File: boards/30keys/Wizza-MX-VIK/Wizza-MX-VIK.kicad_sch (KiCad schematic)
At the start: 88 parts, among them J1 AudioJack4dpb, J2 AudioJack4dpb, J3 Conn_01x03_Socket, J4 Conn_01x03_Socket, J7 Conn_01x05, J8 Conn_01x05, SW1 SW_Push, SW10 SW_Push, SW11 SW_Push, SW12 SW_Push, SW13 SW_Push, SW14 SW_Push, SW15 SW_Push, SW16 SW_Push, SW17 SW_Push, SW18 SW_Push, SW19 SW_Push, SW2 SW_Push, SW20 SW_Push, SW21 SW_Push, SW22 SW_Push, SW23 SW_Push, SW24 SW_Push, SW25 SW_SPDT, SW26 SW_Push, SW27 SW_Push, SW28 SW_Push, SW29 SW_Push, SW3 SW_Push, SW30 SW_SPDT, SW31 SW_Push, SW32 SW_Push, SW33 SW_Push, SW34 Rotary_Encoder_Switch, SW35 Rotary_Encoder_Switch, SW4 SW_Push, SW40 SW_Push, SW5 SW_Push, SW6 SW_Push, SW7 SW_Push, SW8 SW_Push, SW9 SW_Push, U1 Helios, U2 Helios

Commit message: wizza mx vik
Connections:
- net ENC_L_L is gone; now on net EncL_L: SW34.A
- net ENC_L_R is gone; now on net EncL_R: SW35.B
- net ENC_R_L is gone; now on net EncR_L: SW34.B
- net ENC_R_R is gone; now on net EncR_R: SW35.A
- net MISO_L: now also J2.11 (MISO), J6.11 (MISO)
- net MISO_R: now also J1.11 (MISO), J5.11 (MISO)
- net MOSI_L: no longer J2.11 (MISO), J6.11 (MISO)
- net MOSI_R: no longer J1.11 (MISO), J5.11 (MISO)
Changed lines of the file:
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@@
+    )
+  )
+  (global_label "MISO_R" (shape input) (at 386.08 82.55 180) (fields_autoplaced)
+    (effects (font (size 1.27 1.27)) (justify right))
+    (property "Intersheetrefs" "${INTERSHEET_REFS}" (at 376.3404 82.55 0)
+      (effects (font (size 1.27 1.27)) (justify right) hide)
     )
   )
@@
     )
   )
-  (global_label "MOSI_R" (shape input) (at 386.08 82.55 180) (fields_autoplaced)
-    (effects (font (size 1.27 1.27)) (justify right))
-    (property "Intersheetrefs" "${INTERSHEET_REFS}" (at 376.3404 82.55 0)
-      (effects (font (size 1.27 1.27)) (justify right) hide)
-    )
-  )
   (global_label "NCS_L" (shape input) (at 77.47 87.63 0) (fields_autoplaced)
     (effects (font (size 1.27 1.27)) (justify left))
@@
     )
   )
-  (global_label "MOSI_L" (shape input) (at 105.41 118.11 180) (fields_autoplaced)
-    (effects (font (size 1.27 1.27)) (justify right))
-    (property "Intersheetrefs" "${INTERSHEET_REFS}" (at 95.9123 118.11 0)
-      (effects (font (size 1.27 1.27)) (justify right) hide)
-    )
-  )
   (global_label "GND_L" (shape input) (at 179.07 153.67 0) (fields_autoplaced)
     (effects (font (size 1.27 1.27)) (justify left))
@@
     )
   )
-  (global_label "MOSI_R" (shape input) (at 386.08 116.84 180) (fields_autoplaced)
-    (effects (font (size 1.27 1.27)) (justify right))
-    (property "Intersheetrefs" "${INTERSHEET_REFS}" (at 376.3404 116.84 0)
-      (effects (font (size 1.27 1.27)) (justify right) hide)
-    )
-  )
   (global_label "GND_R" (shape input) (at 322.58 66.04 180) (fields_autoplaced)
     (effects (font (size 1.27 1.27)) (justify right))
@@
     )
   )
-  (global_label "ENC_L_R" (shape input) (at 287.02 231.14 270) (fields_autoplaced)
-    (effects (font (size 1.27 1.27)) (justify right))
-    (property "Intersheetrefs" "${INTERSHEET_REFS}" (at 287.02 242.0286 90)
+  (global_label "EncL_R" (shape input) (at 287.02 231.14 270) (fields_autoplaced)
+    (effects (font (size 1.27 1.27)) (justify right))
+    (property "Intersheetrefs" "${INTERSHEET_REFS}" (at 287.02 240.6981 90)
       (effects (font (size 1.27 1.27)) (justify right) hide)
     )
@@
     )
   )
+  (global_label "MISO_L" (shape input) (at 105.41 118.11 180) (fields_autoplaced)
+    (effects (font (size 1.27 1.27)) (justify right))
+    (property "Intersheetrefs" "${INTERSHEET_REFS}" (at 95.9123 118.11 0)
+      (effects (font (size 1.27 1.27)) (justify right) hide)
+    )
+  )
   (global_label "SCLK_R" (shape input) (at 358.14 78.74 0) (fields_autoplaced)
     (effects (font (size 1.27 1.27)) (justify left))
@@
     )
   )
-  (global_label "ENC_L_L" (shape input) (at 146.05 227.33 270) (fields_autoplaced)
-    (effects (font (size 1.27 1.27)) (justify right))
-    (property "Intersheetrefs" "${INTERSHEET_REFS}" (at 146.05 237.9767 90)
+  (global_label "EncL_L" (shape input) (at 146.05 227.33 270) (fields_autoplaced)
+    (effects (font (size 1.27 1.27)) (justify right))
+    (property "Intersheetrefs" "${INTERSHEET_REFS}" (at 146.05 236.6462 90)
       (effects (font (size 1.27 1.27)) (justify right) hide)
     )
@@
     )
   )
+  (global_label "MISO_R" (shape input) (at 386.08 116.84 180) (fields_autoplaced)
+    (effects (font (size 1.27 1.27)) (justify right))
+    (property "Intersheetrefs" "${INTERSHEET_REFS}" (at 376.3404 116.84 0)
+      (effects (font (size 1.27 1.27)) (justify right) hide)
+    )
+  )
   (global_label "EncL_R" (shape input) (at 322.58 60.96 180) (fields_autoplaced)
     (effects (font (size 1.27 1.27)) (justify right))
@@
     )
   )
-  (global_label "ENC_R_R" (shape input) (at 281.94 231.14 270) (fields_autoplaced)
-    (effects (font (size 1.27 1.27)) (justify right))
-    (property "Intersheetrefs" "${INTERSHEET_REFS}" (at 281.94 242.2705 90)
-      (effects (font (size 1.27 1.27)) (justify right) hide)
-    )
-  )
-  (global_label "ENC_R_L" (shape input) (at 151.13 227.33 270) (fields_autoplaced)
-    (effects (font (size 1.27 1.27)) (justify right))
-    (property "Intersheetrefs" "${INTERSHEET_REFS}" (at 151.13 238.2186 90)
-      (effects (font (size 1.27 1.27)) (justify right) hide)
-    )
-  )
-  (global_label "MOSI_L" (shape input) (at 105.41 83.82 180) (fields_autoplaced)
+  (global_label "EncR_R" (shape input) (at 281.94 231.14 270) (fields_autoplaced)
+    (effects (font (size 1.27 1.27)) (justify right))
+    (property "Intersheetrefs" "${INTERSHEET_REFS}" (at 281.94 240.94 90)
+      (effects (font (size 1.27 1.27)) (justify right) hide)
+    )
+  )
+  (global_label "EncR_L" (shape input) (at 151.13 227.33 270) (fields_autoplaced)
+    (effects (font (size 1.27 1.27)) (justify right))
+    (property "Intersheetrefs" "${INTERSHEET_REFS}" (at 151.13 236.8881 90)
+      (effects (font (size 1.27 1.27)) (justify right) hide)
+    )
+  )
+  (global_label "MISO_L" (shape input) (at 105.41 83.82 180) (fields_autoplaced)
     (effects (font (size 1.27 1.27)) (justify right))
     (property "Intersheetrefs" "${INTERSHEET_REFS}" (at 95.9123 83.82 0)

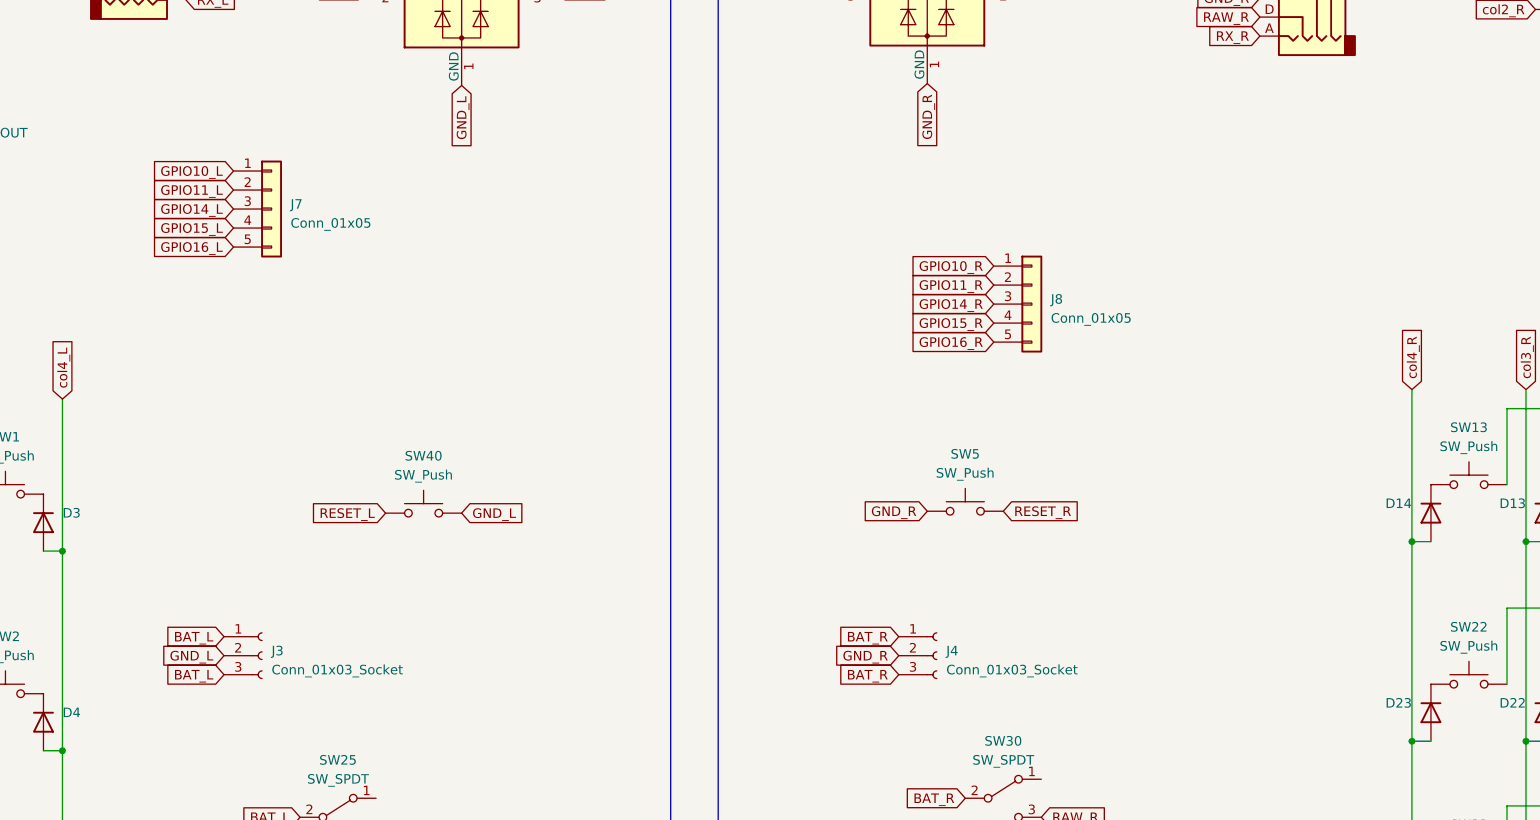
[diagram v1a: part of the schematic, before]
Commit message: add vik 18 pin ffc
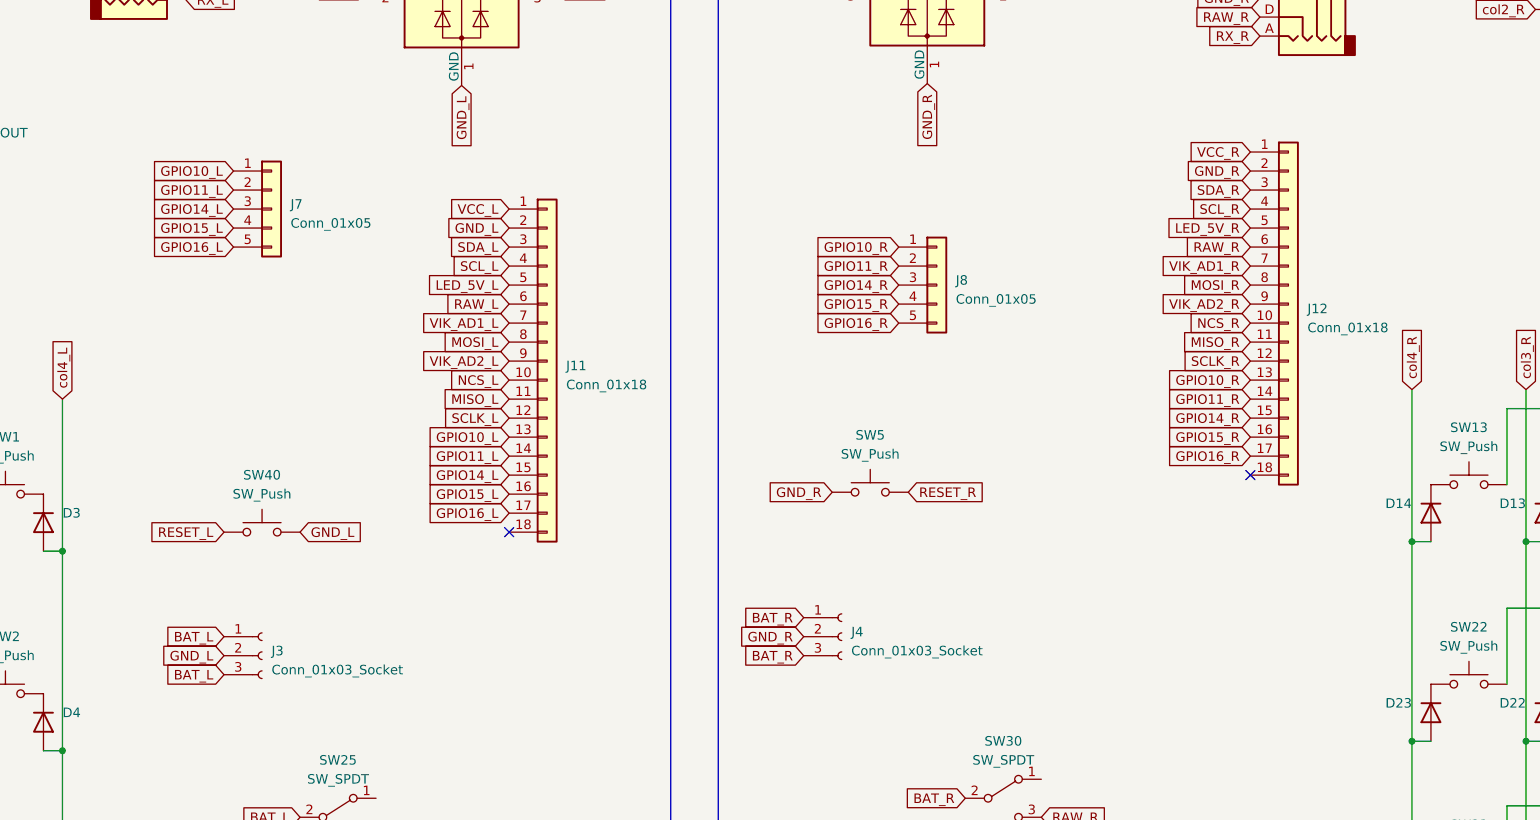
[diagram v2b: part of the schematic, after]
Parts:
- added J11, J12: Conn_01x18, Alaa:FPC-SMD_FPC05018-09200-.5mm-rev, symbol Connector_Generic:Conn_01x18
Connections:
- net GND_L: now also J11.2 (Pin_2)
- net GND_R: now also J12.2 (Pin_2)
- net GPIO10_L: now also J11.13 (Pin_13)
- net GPIO10_R: now also J12.13 (Pin_13)
- net GPIO11_L: now also J11.14 (Pin_14)
- net GPIO11_R: now also J12.14 (Pin_14)
- net GPIO14_L: now also J11.15 (Pin_15)
- net GPIO14_R: now also J12.15 (Pin_15)
- net GPIO15_L: now also J11.16 (Pin_16)
- net GPIO15_R: now also J12.16 (Pin_16)
- net GPIO16_L: now also J11.17 (Pin_17)
- net GPIO16_R: now also J12.17 (Pin_17)
- net LED_5V_L: now also J11.5 (Pin_5)
- net LED_5V_R: now also J12.5 (Pin_5)
- net MISO_L: now also J11.11 (Pin_11)
- net MISO_R: now also J12.11 (Pin_11)
- net MOSI_L: now also J11.8 (Pin_8)
- net MOSI_R: now also J12.8 (Pin_8)
- net NCS_L: now also J11.10 (Pin_10)
- net NCS_R: now also J12.10 (Pin_10)
- net RAW_L: now also J11.6 (Pin_6)
- net RAW_R: now also J12.6 (Pin_6)
- net SCLK_L: now also J11.12 (Pin_12)
- net SCLK_R: now also J12.12 (Pin_12)
- net SCL_L: now also J11.4 (Pin_4)
- net SCL_R: now also J12.4 (Pin_4)
- net SDA_L: now also J11.3 (Pin_3)
- net SDA_R: now also J12.3 (Pin_3)
- net VCC_L: now also J11.1 (Pin_1)
- net VCC_R: now also J12.1 (Pin_1)
- net VIK_AD1_L: now also J11.7 (Pin_7)
- net VIK_AD1_R: now also J12.7 (Pin_7)
- net VIK_AD2_L: now also J11.9 (Pin_9)
- net VIK_AD2_R: now also J12.9 (Pin_9)
- no-connect marks 4 -> 6
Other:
- moved on the sheet: J4, J8, SW40, SW5
